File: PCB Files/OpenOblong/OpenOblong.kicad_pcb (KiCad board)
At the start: 2 copper layers, 282.7 x 136.2 mm, 91 parts, among them J1 USB C Connector, J2 JTAG_TC2030, SW1 Boot, SW10 MX_SW_solder, SW11 MX_SW_HS, SW12 MX_SW_solder, SW13 MX_SW_HS, SW14 MX_SW_HS, SW15 MX_SW_solder, SW16 MX_SW_HS, SW17 MX_SW_solder, SW18 MX_SW_HS, SW19 MX_SW_solder, SW2 MX_SW_HS, SW20 MX_SW_solder, SW21 MX_SW_HS, SW22 MX_SW_HS, SW23 MX_SW_solder, SW24 MX_SW_HS, SW25 MX_SW_solder, SW26 MX_SW_HS, SW27 MX_SW_solder, SW28 MX_SW_HS, SW29 MX_SW_solder, SW3 MX_SW_solder, SW30 MX_SW_solder, SW31 MX_SW_HS, SW32 MX_SW_HS, SW33 MX_SW_solder, SW34 MX_SW_HS, SW35 MX_SW_solder, SW36 MX_SW_HS, SW37 MX_SW_solder, SW38 MX_SW_solder, SW39 MX_SW_HS, SW4 MX_SW_solder, SW40 MX_SW_HS, SW41 MX_SW_solder, SW44 MX_SW_HS, SW45 MX_SW_solder, SW5 MX_SW_HS, SW6 MX_SW_HS, SW7 MX_SW_solder, SW8 MX_SW_solder, SW9 MX_SW_HS, U1 XC6206, U2 USBLC6-2SC6, U3 RP2040, U4 W25Q128JVS, Y1 12MHz

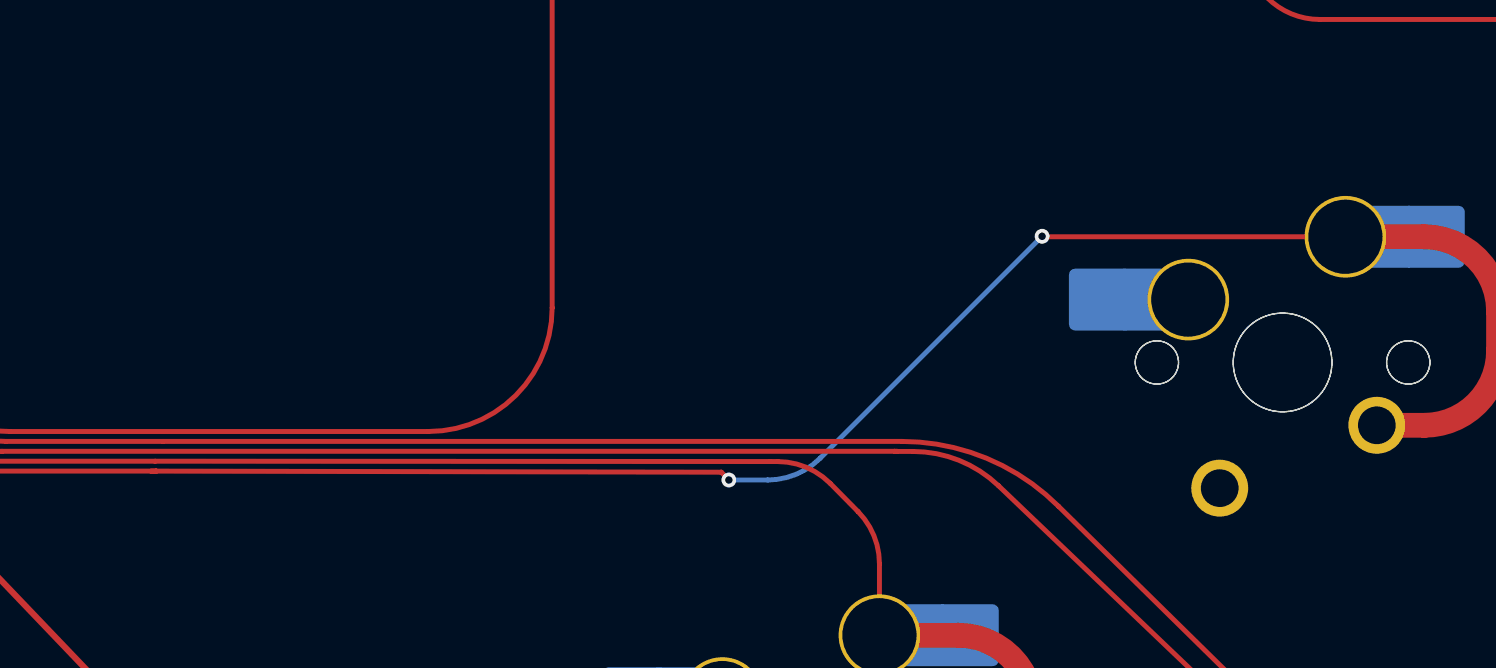
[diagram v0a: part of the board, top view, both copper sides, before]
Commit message: changed c-up wiring
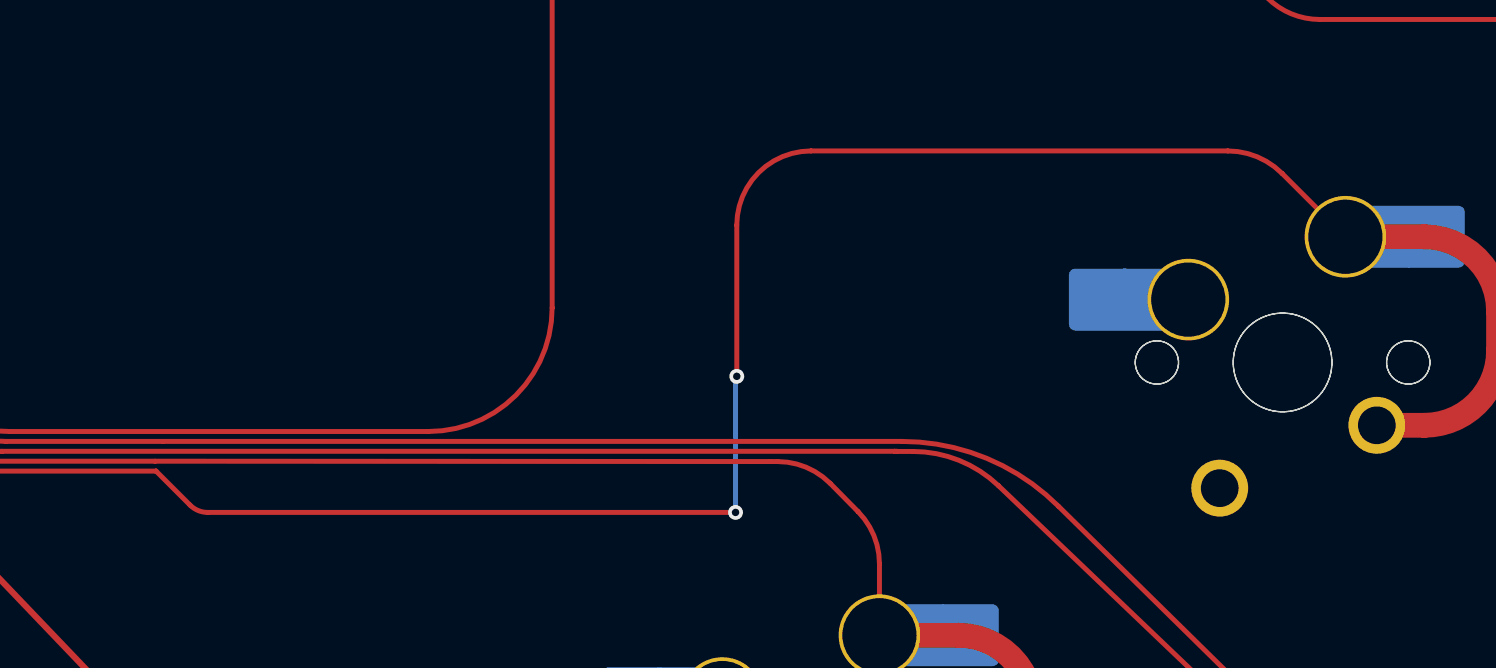
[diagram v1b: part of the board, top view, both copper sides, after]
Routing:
- net C_UP: track 153.9 -> 164.7 mm
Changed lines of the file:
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@@
     (fp_arc (start 2.494322 0.86022) (mid 1.670693 2.183637) (end 0.2 2.70022)
       (stroke (width 0.15) (type solid)) (layer "B.SilkS"))
-    (fp_arc (start 6.085176 4.75022) (mid 5.499392 6.164436) (end 4.085176 6.75022)
+    (fp_arc (start 6.085176 4.75022) (mid 5.499393 6.164439) (end 4.085176 6.75022)
       (stroke (width 0.15) (type solid)) (layer "B.SilkS"))
     (fp_line (start -9.525 -9.525) (end -9.525 9.525)
@@
     (fp_arc (start 2.494322 0.86022) (mid 1.670502 2.183399) (end 0.2 2.70022)
       (stroke (width 0.05) (type solid)) (layer "B.CrtYd"))
-    (fp_arc (start 6.085176 4.75022) (mid 5.499392 6.164436) (end 4.085176 6.75022)
+    (fp_arc (start 6.085176 4.75022) (mid 5.499393 6.164439) (end 4.085176 6.75022)
       (stroke (width 0.05) (type solid)) (layer "B.CrtYd"))
     (fp_line (start -7 -7) (end -7 7)
@@
   (arc (start 183.439303 157.447387) (mid 185.560623 156.568707) (end 186.439303 154.447386) (width 1) (layer "F.Cu") (net 8))
   (segment (start 234.448565 104.028961) (end 237.636565 104.02896) (width 1) (layer "F.Cu") (net 9))
-  (segment (start 186.172136 113.5) (end 186.38 113.500404) (width 0.2) (layer "F.Cu") (net 9))
-  (segment (start 209.53 113.86) (end 209.54 113.86) (width 0.2) (layer "F.Cu") (net 9))
-  (segment (start 222.20896 104.02896) (end 234.448565 104.02896) (width 0.2) (layer "F.Cu") (net 9))
   (segment (start 188.538525 60.095591) (end 166.860304 81.773812) (width 0.2) (layer "F.Cu") (net 9))
+  (segment (start 186.38 113.500404) (end 187.756703 114.877107) (width 0.2) (layer "F.Cu") (net 9))
   (segment (start 166.860304 104.680304) (end 172.751068 110.571068) (width 0.2) (layer "F.Cu") (net 9))
   (segment (start 194.552062 58.924018) (end 191.366952 58.924018) (width 0.2) (layer "F.Cu") (net 9))
-  (segment (start 222.19 104.01) (end 222.20896 104.02896) (width 0.2) (layer "F.Cu") (net 9))
-  (segment (start 186.38 113.500404) (end 209.222766 113.54479) (width 0.2) (layer "F.Cu") (net 9))
-  (segment (start 209.222766 113.54479) (end 209.22479 113.54479) (width 0.2) (layer "F.Cu") (net 9))
+  (segment (start 188.46381 115.17) (end 209.8 115.17) (width 0.2) (layer "F.Cu") (net 9))
+  (segment (start 209.85 109.67) (end 209.85 103.56) (width 0.2) (layer "F.Cu") (net 9))
   (segment (start 163.931372 88.84488) (end 163.931372 97.609236) (width 0.2) (layer "F.Cu") (net 9))
-  (segment (start 209.54 113.86) (end 209.51 113.83) (width 0.2) (layer "F.Cu") (net 9))
-  (segment (start 209.22479 113.54479) (end 209.53 113.85) (width 0.2) (layer "F.Cu") (net 9))
+  (segment (start 231.88786 101.468255) (end 234.448565 104.02896) (width 0.2) (layer "F.Cu") (net 9))
+  (segment (start 212.85 100.56) (end 229.695139 100.56) (width 0.2) (layer "F.Cu") (net 9))
   (segment (start 186.379596 113.5) (end 186.38 113.500404) (width 0.2) (layer "F.Cu") (net 9))
   (segment (start 179.822136 113.5) (end 186.379596 113.5) (width 0.2) (layer "F.Cu") (net 9))
   (segment (start 237.636565 111.64896) (end 235.718565 111.64896) (width 1) (layer "F.Cu") (net 9))
   (segment (start 240.636565 107.02896) (end 240.636565 108.648961) (width 1) (layer "F.Cu") (net 9))
-  (segment (start 209.53 113.85) (end 209.53 113.86) (width 0.2) (layer "F.Cu") (net 9))
-  (via (at 222.19 104.01) (size 0.6) (drill 0.3) (layers "F.Cu" "B.Cu") (net 9))
-  (via (at 209.53 113.86) (size 0.6) (drill 0.3) (layers "F.Cu" "B.Cu") (net 9))
+  (via (at 209.85 109.67) (size 0.6) (drill 0.3) (layers "F.Cu" "B.Cu") (net 9))
+  (via (at 209.8 115.17) (size 0.6) (drill 0.3) (layers "F.Cu" "B.Cu") (net 9))
   (arc (start 237.636565 111.64896) (mid 239.757885 110.770281) (end 240.636565 108.648961) (width 1) (layer "F.Cu") (net 9))
   (arc (start 195.98 58.3325) (mid 195.324814 58.770308) (end 194.552062 58.924018) (width 0.2) (layer "F.Cu") (net 9))
   (arc (start 240.636565 107.02896) (mid 239.757885 104.90764) (end 237.636565 104.02896) (width 1) (layer "F.Cu") (net 9))
+  (arc (start 212.85 100.56) (mid 210.72868 101.43868) (end 209.85 103.56) (width 0.2) (layer "F.Cu") (net 9))
   (arc (start 163.931372 97.609236) (mid 164.692577 101.43607) (end 166.860304 104.680304) (width 0.2) (layer "F.Cu") (net 9))
   (arc (start 191.366952 58.924018) (mid 189.836218 59.2285) (end 188.538525 60.095591) (width 0.2) (layer "F.Cu") (net 9))
   (arc (start 172.751068 110.571068) (mid 175.995302 112.738795) (end 179.822136 113.5) (width 0.2) (layer "F.Cu") (net 9))
+  (arc (start 229.695139 100.56) (mid 230.881831 100.796048) (end 231.88786 101.468255) (width 0.2) (layer "F.Cu") (net 9))
   (arc (start 166.860304 81.773812) (mid 164.692576 85.018046) (end 163.931372 88.84488) (width 0.2) (layer "F.Cu") (net 9))
-  (segment (start 222.19 104.01) (end 213.21868 112.98132) (width 0.2) (layer "B.Cu") (net 9))
-  (segment (start 211.097359 113.86) (end 209.53 113.86) (width 0.2) (layer "B.Cu") (net 9))
-  (arc (start 213.21868 112.98132) (mid 212.24541 113.631638) (end 211.097359 113.86) (width 0.2) (layer "B.Cu") (net 9))
+  (arc (start 188.46381 115.17) (mid 188.081127 115.09388) (end 187.756703 114.877107) (width 0.2) (layer "F.Cu") (net 9))
+  (segment (start 209.8 115.17) (end 209.8 109.72) (width 0.2) (layer "B.Cu") (net 9))
+  (segment (start 209.8 109.72) (end 209.85 109.67) (width 0.2) (layer "B.Cu") (net 9))
   (segment (start 166.599175 103.7892) (end 167.030755 104.281324) (width 0.2) (layer "F.Cu") (net 10))
   (segment (start 173.150011 110.400656) (end 173.642137 110.832238) (width 0.2) (layer "F.Cu") (net 10))
